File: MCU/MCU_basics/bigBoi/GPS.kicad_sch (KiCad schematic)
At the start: 8 parts, among them J1 Conn_Coaxial

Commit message: Schematic pins assignment
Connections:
- net GPS_RX_N: now also U?.H1 (RX); no longer U?.G1 (TX)
- net GPS_TX_N: now also U?.G1 (TX); no longer U?.H1 (RX)
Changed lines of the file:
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@@
 		)
 	)
-	(label "GPS_RX_N"
+	(label "GPS_TX_N"
 		(at 90.17 100.33 0)
 		(effects
@@
 		)
 	)
-	(label "GPS_TX_N"
+	(label "GPS_RX_N"
 		(at 90.17 102.87 0)
 		(effects

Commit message: schematic connections
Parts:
- gave numbers to parts that had none: 1
- renumbered C1 to C35, C2 to C36, C3 to C37, J1 to J2, R1 to R3
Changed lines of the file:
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@@
 		(dnp no)
 		(fields_autoplaced yes)
-		(property "Reference" "#PWR035"
+		(property "Reference" "#PWR052"
 			(at 152.4 106.68 0)
 			(hide yes)
@@
 			(project "bigBoi"
 				(path "/0a118c22-2522-42a6-b7a6-70c79326ece4/a4e29843-7119-4d54-a27a-f8cdecaec2b9"
-					(reference "#PWR035")
+					(reference "#PWR052")
 					(unit 1)
 				)
@@
 		(dnp no)
 		(fields_autoplaced yes)
-		(property "Reference" "#PWR033"
+		(property "Reference" "#PWR050"
 			(at 120.65 152.4 0)
 			(hide yes)
@@
 			(project "bigBoi"
 				(path "/0a118c22-2522-42a6-b7a6-70c79326ece4/a4e29843-7119-4d54-a27a-f8cdecaec2b9"
-					(reference "#PWR033")
+					(reference "#PWR050")
 					(unit 1)
 				)
@@
 		(in_pos_files yes)
 		(dnp no)
-		(property "Reference" "R1"
+		(property "Reference" "R3"
 			(at 127 62.484 0)
 			(show_name no)
@@
 			(project "bigBoi"
 				(path "/0a118c22-2522-42a6-b7a6-70c79326ece4/a4e29843-7119-4d54-a27a-f8cdecaec2b9"
-					(reference "R1")
+					(reference "R3")
 					(unit 1)
 				)
@@
 		(dnp no)
 		(fields_autoplaced yes)
-		(property "Reference" "J1"
+		(property "Reference" "J2"
 			(at 156.21 94.2731 0)
 			(show_name no)
@@
 			(project "bigBoi"
 				(path "/0a118c22-2522-42a6-b7a6-70c79326ece4/a4e29843-7119-4d54-a27a-f8cdecaec2b9"
-					(reference "J1")
+					(reference "J2")
 					(unit 1)
 				)
@@
 		(in_pos_files yes)
 		(dnp no)
-		(property "Reference" "U?"
+		(property "Reference" "U5"
 			(at 122.7933 143.51 0)
 			(hide yes)
@@
 			(project "bigBoi"
 				(path "/0a118c22-2522-42a6-b7a6-70c79326ece4/a4e29843-7119-4d54-a27a-f8cdecaec2b9"
-					(reference "U?")
+					(reference "U5")
 					(unit 1)
 				)
@@
 		(in_pos_files yes)
 		(dnp no)
-		(property "Reference" "C1"
+		(property "Reference" "C35"
 			(at 110.744 72.644 0)
 			(show_name no)
@@
 			(project "bigBoi"
 				(path "/0a118c22-2522-42a6-b7a6-70c79326ece4/a4e29843-7119-4d54-a27a-f8cdecaec2b9"
-					(reference "C1")
+					(reference "C35")
 					(unit 1)
 				)
@@
 		(dnp no)
 		(fields_autoplaced yes)
-		(property "Reference" "#PWR032"
+		(property "Reference" "#PWR049"
 			(at 116.84 74.93 0)
 			(hide yes)
@@
 			(project "bigBoi"
 				(path "/0a118c22-2522-42a6-b7a6-70c79326ece4/a4e29843-7119-4d54-a27a-f8cdecaec2b9"
-					(reference "#PWR032")
+					(reference "#PWR049")
 					(unit 1)
 				)
@@
 		(dnp no)
 		(fields_autoplaced yes)
-		(property "Reference" "#PWR034"
+		(property "Reference" "#PWR051"
 			(at 128.27 66.04 0)
 			(hide yes)
@@
 			(project "bigBoi"
 				(path "/0a118c22-2522-42a6-b7a6-70c79326ece4/a4e29843-7119-4d54-a27a-f8cdecaec2b9"
-					(reference "#PWR034")
+					(reference "#PWR051")
 					(unit 1)
 				)
@@
 		(in_pos_files yes)
 		(dnp no)
-		(property "Reference" "C2"
+		(property "Reference" "C36"
 			(at 120.65 72.898 0)
 			(show_name no)
@@
 			(project "bigBoi"
 				(path "/0a118c22-2522-42a6-b7a6-70c79326ece4/a4e29843-7119-4d54-a27a-f8cdecaec2b9"
-					(reference "C2")
+					(reference "C36")
 					(unit 1)
 				)
@@
 		(in_pos_files yes)
 		(dnp no)
-		(property "Reference" "C3"
+		(property "Reference" "C37"
 			(at 129.286 71.374 0)
 			(show_name no)
@@
 			(project "bigBoi"
 				(path "/0a118c22-2522-42a6-b7a6-70c79326ece4/a4e29843-7119-4d54-a27a-f8cdecaec2b9"
-					(reference "C3")
-					(unit 1)
-				)
+					(reference "C37")
+					(unit 1)
+				)

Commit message: ERC resolving
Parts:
- C35, C37: footprint (none) -> Capacitor_SMD:C_0402_1005Metric
- C36: footprint (none) -> Capacitor_SMD:C_0603_1608Metric
- R3: footprint (none) -> Resistor_SMD:R_0402_1005Metric
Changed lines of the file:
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@@
-	(wire
-		(pts
-			(xy 90.17 123.19) (xy 105.41 123.19)
-		)
-		(stroke
-			(width 0)
-			(type default)
-		)
-	)
 	(wire
 		(pts
@@
 	(wire
 		(pts
-			(xy 90.17 107.95) (xy 105.41 107.95)
-		)
-		(stroke
-			(width 0)
-			(type default)
-		)
-	)
-	(wire
-		(pts
-			(xy 87.63 110.49) (xy 105.41 110.49)
-		)
-		(stroke
-			(width 0)
-			(type default)
-		)
-	)
-	(wire
-		(pts
 			(xy 83.82 82.55) (xy 83.82 128.27)
 		)
@@
 	(wire
 		(pts
-			(xy 90.17 102.87) (xy 105.41 102.87)
-		)
-		(stroke
-			(width 0)
-			(type default)
-		)
-	)
-	(wire
-		(pts
 			(xy 120.65 82.55) (xy 120.65 85.09)
 		)
@@
 	(wire
 		(pts
-			(xy 90.17 100.33) (xy 105.41 100.33)
-		)
-		(stroke
-			(width 0)
-			(type default)
-		)
-	)
-	(wire
-		(pts
 			(xy 114.3 71.12) (xy 116.84 71.12)
 		)
@@
 		)
 	)
-	(label "GPS_WAKE_N"
-		(at 90.17 107.95 0)
+	(global_label "GPS_TX_N"
+		(shape input)
+		(at 105.41 100.33 180)
+		(fields_autoplaced yes)
 		(effects
 			(font
 				(size 1.27 1.27)
 			)
-			(justify left bottom)
-		)
-	)
-	(label "GPS_TX_N"
-		(at 90.17 100.33 0)
+			(justify right)
+		)
+		(property "Intersheetrefs" "${INTERSHEET_REFS}"
+			(at 93.2325 100.33 0)
+			(hide yes)
+			(show_name no)
+			(do_not_autoplace no)
+			(effects
+				(font
+					(size 1.27 1.27)
+				)
+				(justify right)
+			)
+		)
+	)
+	(global_label "GPS_RX_N"
+		(shape input)
+		(at 105.41 102.87 180)
+		(fields_autoplaced yes)
 		(effects
 			(font
 				(size 1.27 1.27)
 			)
-			(justify left bottom)
-		)
-	)
-	(label "GPS_RX_N"
-		(at 90.17 102.87 0)
+			(justify right)
+		)
+		(property "Intersheetrefs" "${INTERSHEET_REFS}"
+			(at 92.9301 102.87 0)
+			(hide yes)
+			(show_name no)
+			(do_not_autoplace no)
+			(effects
+				(font
+					(size 1.27 1.27)
+				)
+				(justify right)
+			)
+		)
+	)
+	(global_label "GPS_TIMEPULSE_N"
+		(shape input)
+		(at 105.41 110.49 180)
+		(fields_autoplaced yes)
 		(effects
 			(font
 				(size 1.27 1.27)
 			)
-			(justify left bottom)
-		)
-	)
-	(label "GPS_TIMEPULSE_N"
-		(at 87.63 110.49 0)
+			(justify right)
+		)
+		(property "Intersheetrefs" "${INTERSHEET_REFS}"
+			(at 85.2497 110.49 0)
+			(hide yes)
+			(show_name no)
+			(do_not_autoplace no)
+			(effects
+				(font
+					(size 1.27 1.27)
+				)
+				(justify right)
+			)
+		)
+	)
+	(global_label "GPS_RESET_N"
+		(shape input)
+		(at 105.41 123.19 180)
+		(fields_autoplaced yes)
 		(effects
 			(font
 				(size 1.27 1.27)
 			)
-			(justify left bottom)
-		)
-	)
-	(label "GPS_RESET_N"
-		(at 90.17 123.19 0)
+			(justify right)
+		)
+		(property "Intersheetrefs" "${INTERSHEET_REFS}"
+			(at 89.6645 123.19 0)
+			(hide yes)
+			(show_name no)
+			(do_not_autoplace no)
+			(effects
+				(font
+					(size 1.27 1.27)
+				)
+				(justify right)
+			)
+		)
+	)
+	(global_label "GPS_WAKE_N"
+		(shape input)
+		(at 105.41 107.95 180)
+		(fields_autoplaced yes)
 		(effects
 			(font
 				(size 1.27 1.27)
 			)
-			(justify left bottom)
+			(justify right)
+		)
+		(property "Intersheetrefs" "${INTERSHEET_REFS}"
+			(at 90.4506 107.95 0)
+			(hide yes)
+			(show_name no)
+			(do_not_autoplace no)
+			(effects
+				(font
+					(size 1.27 1.27)
+				)
+				(justify right)
+			)
 		)
 	)
@@
 			)
 		)
-		(property "Footprint" ""
+		(property "Footprint" "Resistor_SMD:R_0402_1005Metric"
 			(at 123.952 63.5 90)
 			(hide yes)
@@
 			)
 		)
-		(property "Footprint" ""
+		(property "Footprint" "Capacitor_SMD:C_0402_1005Metric"
 			(at 115.2652 78.74 0)
 			(hide yes)
@@
 			)
 		)
-		(property "Footprint" ""
+		(property "Footprint" "Capacitor_SMD:C_0603_1608Metric"
 			(at 120.3452 78.74 0)
 			(hide yes)
@@
 			)
 		)
-		(property "Footprint" ""
+		(property "Footprint" "Capacitor_SMD:C_0402_1005Metric"
 			(at 124.7648 67.31 0)
 			(hide yes)

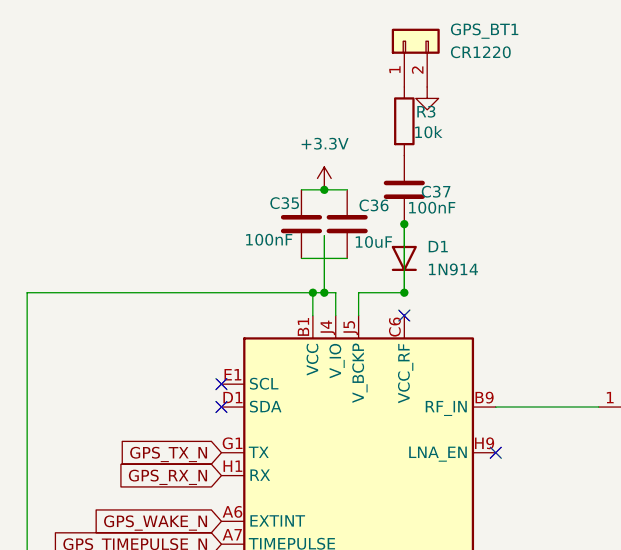
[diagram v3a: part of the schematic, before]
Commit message: most footprints assigned
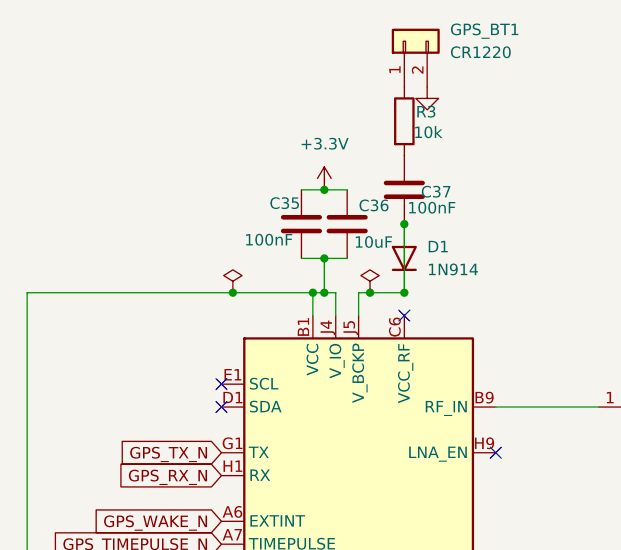
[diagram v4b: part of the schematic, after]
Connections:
- net at U5.B1 (VCC), U5.J4 (V_IO), U5.J6 (VIO_SEL): now also C35.2, C36.2
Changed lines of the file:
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@@
 	(paper "A4")
+	(junction
+		(at 116.84 78.74)
+		(diameter 0)
+		(color 0 0 0 0)
+	)
 	(junction
 		(at 125.73 74.93)
@@
 	)
 	(junction
+		(at 115.57 82.55)
+		(diameter 0)
+		(color 0 0 0 0)
+	)
+	(junction
 		(at 116.84 82.55)
 		(diameter 0)
@@
 	)
 	(junction
-		(at 115.57 82.55)
+		(at 121.92 82.55)
 		(diameter 0)
 		(color 0 0 0 0)
@@
 		(color 0 0 0 0)
 	)
+	(junction
+		(at 106.68 82.55)
+		(diameter 0)
+		(color 0 0 0 0)
+	)
 	(no_connect
 		(at 105.41 95.25)
@@
 	(wire
 		(pts
-			(xy 120.65 82.55) (xy 125.73 82.55)
+			(xy 120.65 82.55) (xy 121.92 82.55)
 		)
 		(stroke
@@
 	(wire
 		(pts
+			(xy 116.84 78.74) (xy 119.38 78.74)
+		)
+		(stroke
+			(width 0)
+			(type default)
+		)
+	)
+	(wire
+		(pts
+			(xy 116.84 78.74) (xy 116.84 82.55)
+		)
+		(stroke
+			(width 0)
+			(type default)
+		)
+	)
+	(wire
+		(pts
 			(xy 83.82 82.55) (xy 83.82 128.27)
 		)
@@
 	(wire
 		(pts
-			(xy 116.84 76.2) (xy 116.84 82.55)
+			(xy 121.92 82.55) (xy 125.73 82.55)
+		)
+		(stroke
+			(width 0)
+			(type default)
+		)
+	)
+	(wire
+		(pts
+			(xy 106.68 82.55) (xy 83.82 82.55)
 		)
 		(stroke
@@
 	(wire
 		(pts
-			(xy 115.57 82.55) (xy 83.82 82.55)
-		)
-		(stroke
-			(width 0)
-			(type default)
-		)
-	)
-	(wire
-		(pts
-			(xy 114.3 78.74) (xy 119.38 78.74)
+			(xy 115.57 82.55) (xy 106.68 82.55)
+		)
+		(stroke
+			(width 0)
+			(type default)
+		)
+	)
+	(wire
+		(pts
+			(xy 114.3 78.74) (xy 116.84 78.74)
 		)
 		(stroke
@@
 				(path "/0a118c22-2522-42a6-b7a6-70c79326ece4/a4e29843-7119-4d54-a27a-f8cdecaec2b9"
 					(reference "#PWR050")
+					(unit 1)
+				)
+			)
+		)
+	)
+	(symbol
+		(lib_id "power:PWR_FLAG")
+		(at 106.68 82.55 0)
+		(unit 1)
+		(body_style 1)
+		(exclude_from_sim no)
+		(in_bom yes)
+		(on_board yes)
+		(in_pos_files yes)
+		(dnp no)
+		(fields_autoplaced yes)
+		(property "Reference" "#FLG02"
+			(at 106.68 80.645 0)
+			(hide yes)
+			(show_name no)
+			(do_not_autoplace no)
+			(effects
+				(font
+					(size 1.27 1.27)
+				)
+			)
+		)
+		(property "Value" "PWR_FLAG"
+			(at 106.68 77.47 0)
+			(hide yes)
+			(show_name no)
+			(do_not_autoplace no)
+			(effects
+				(font
+					(size 1.27 1.27)
+				)
+			)
+		)
+		(property "Footprint" ""
+			(at 106.68 82.55 0)
+			(hide yes)
+			(show_name no)
+			(do_not_autoplace no)
+			(effects
+				(font
+					(size 1.27 1.27)
+				)
+			)
+		)
+		(property "Datasheet" ""
+			(at 106.68 82.55 0)
+			(hide yes)
+			(show_name no)
+			(do_not_autoplace no)
+			(effects
+				(font
+					(size 1.27 1.27)
+				)
+			)
+		)
+		(property "Description" "Special symbol for telling ERC where power comes from"
+			(at 106.68 82.55 0)
+			(hide yes)
+			(show_name no)
+			(do_not_autoplace no)
+			(effects
+				(font
+					(size 1.27 1.27)
+				)
+			)
+		)
+		(pin "1"
+		)
+		(instances
+			(project "bigBoi"
+				(path "/0a118c22-2522-42a6-b7a6-70c79326ece4/a4e29843-7119-4d54-a27a-f8cdecaec2b9"
+					(reference "#FLG02")
 					(unit 1)
 				)
@@
 					(unit 1)
 				)
+			)
+		)
+	)
+	(symbol
+		(lib_id "power:PWR_FLAG")
+		(at 121.92 82.55 0)
+		(unit 1)
+		(body_style 1)
+		(exclude_from_sim no)
+		(in_bom yes)
+		(on_board yes)
+		(in_pos_files yes)
+		(dnp no)
+		(fields_autoplaced yes)
+		(property "Reference" "#FLG01"
+			(at 121.92 80.645 0)
+			(hide yes)
+			(show_name no)
+			(do_not_autoplace no)
+			(effects
+				(font
+					(size 1.27 1.27)
+				)
+			)
+		)
+		(property "Value" "PWR_FLAG"
+			(at 121.92 77.47 0)
+			(hide yes)
+			(show_name no)
+			(do_not_autoplace no)
+			(effects
+				(font
+					(size 1.27 1.27)
+				)
+			)
+		)
+		(property "Footprint" ""
+			(at 121.92 82.55 0)
+			(hide yes)
+			(show_name no)
+			(do_not_autoplace no)
+			(effects
+				(font
+					(size 1.27 1.27)
+				)
+			)
+		)
+		(property "Datasheet" ""
+			(at 121.92 82.55 0)
+			(hide yes)
+			(show_name no)
+			(do_not_autoplace no)
+			(effects
+				(font
+					(size 1.27 1.27)
+				)
+			)
+		)
+		(property "Description" "Special symbol for telling ERC where power comes from"
+			(at 121.92 82.55 0)
+			(hide yes)
+			(show_name no)
+			(do_not_autoplace no)
+			(effects
+				(font
+					(size 1.27 1.27)
+				)
+			)
+		)
+		(pin "1"
+		)
+		(instances
+			(project "bigBoi"
+				(path "/0a118c22-2522-42a6-b7a6-70c79326ece4/a4e29843-7119-4d54-a27a-f8cdecaec2b9"
+					(reference "#FLG01")
+					(unit 1)
+				)

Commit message: small changes
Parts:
- J2: footprint (none) -> Connector_Coaxial:U.FL_Hirose_U.FL-R-SMT-1_Vertical
- U5: footprint Package_LGA:ublox_LGA-53_4.5x4.5mm_Layout9x9_P0.5mm -> Nebula-footprints:MIA-M10Q
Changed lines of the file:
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@@
 			)
 		)
-		(property "Footprint" ""
+		(property "Footprint" "Connector_Coaxial:U.FL_Hirose_U.FL-R-SMT-1_Vertical"
 			(at 152.4 95.25 0)
 			(hide yes)
@@
 			)
 		)
-		(property "Footprint" "Package_LGA:ublox_LGA-53_4.5x4.5mm_Layout9x9_P0.5mm"
+		(property "Footprint" "Nebula-footprints:MIA-M10Q"
 			(at 120.65 115.57 0)
 			(hide yes)

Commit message: Y2 fixed
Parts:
- GPS_BT1: footprint (none) -> Battery:BatteryHolder_Keystone_500
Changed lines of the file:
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@@
 			)
 		)
-		(property "Footprint" ""
+		(property "Footprint" "Battery:BatteryHolder_Keystone_500"
 			(at 125.73 54.61 0)
 			(hide yes)

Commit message: routing complete
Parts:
- removed D1: 1N914, Diode_THT:D_DO-35_SOD27_P7.62mm_Horizontal, symbol Diode:1N914
- removed GPS_BT1: CR1220, Battery:BatteryHolder_Keystone_500, symbol Connector_Generic:Conn_01x02
- added BT2: Battery, Battery:BatteryHolder_LINX_BAT-HLD-012-SMT, symbol Device:Battery
- added C61, C62: 100nF, Capacitor_SMD:C_0402_1005Metric, symbol Device:C
- added D3: BAT54, Diode_SMD:D_0402_1005Metric, symbol Device:D
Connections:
- net +3.3V: now also C61.1, C62.1
- net GND: now also BT2.2 (-)
- net at R3.1: now also BT2.1 (+)
- net at U5.J5 (V_BCKP): now also D3.1 (K); no longer C37.1
- net at C35.2, C36.2, U5.B1 (VCC)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: now also C61.2, C62.2
- new net: C37.1, D3.2 (A)
